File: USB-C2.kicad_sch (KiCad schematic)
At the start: 85 parts, among them J4 USB_C_Receptacle, J5 I2C2_TPS, J6 I2C, SW2 FW_Upgrade, U10 M24256-BWMN6P, U11 TPD4E02B04DQA, U12 TPD4E02B04DQA, U13 TPD4E02B04DQA, U14 TUSB1142IRNQR_C5216209, U8 TVS2200DRV, U9 TPS25762CQRQLRQ1

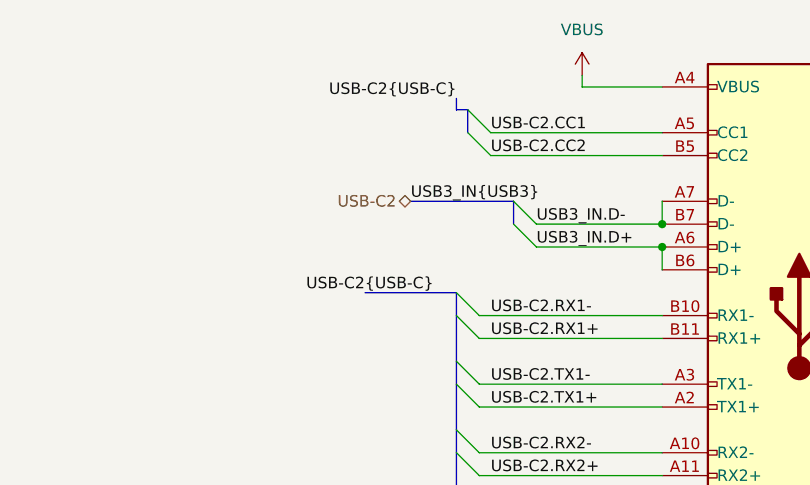
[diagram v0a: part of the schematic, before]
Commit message: labels naming fixes, USB Type E connector added
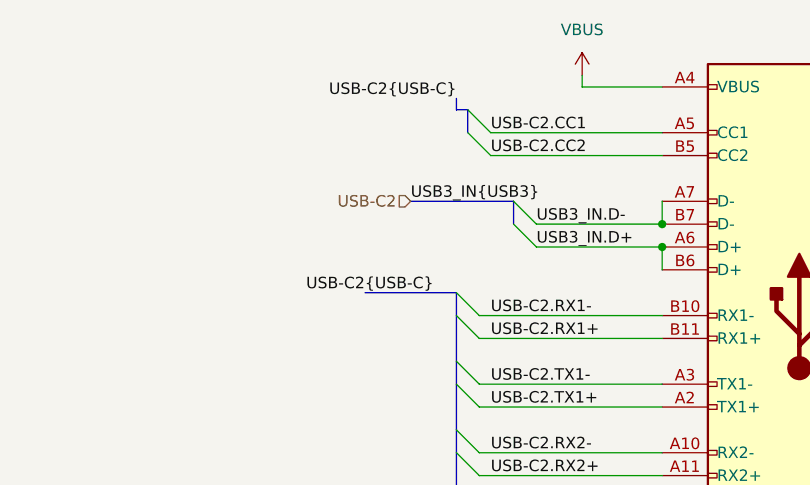
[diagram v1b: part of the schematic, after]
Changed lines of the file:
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@@
 	)
 	(hierarchical_label "USB-C2"
-		(shape bidirectional)
+		(shape input)
 		(at 334.01 34.29 180)
 		(effects

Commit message: TPS25762 EEPROM connector added
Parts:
- added J7: I2C_EEPROM, symbol Connector:Conn_01x02_Pin
- added R26: 1k DNP, symbol Device:R
- J5: value I2C2_TPS -> I2C2_PD_Controller
- J6: value I2C -> I2C_Mux
- renumbered C46 to C45, C45 to C46, C54 to C53, C55 to C54, C53 to C55, R13 to R12, R14 to R13, R15 to R14, R16 to R15, R17 to R16, R18 to R17, R21 to R18, R22 to R21, R23 to R22, R24 to R23, R25 to R24, R26 to R25, R35 to R27, R27 to R28, R28 to R29, R29 to R30, R36 to R31, R37 to R32, R30 to R33, R31 to R34, R32 to R35, R38 to R36, R39 to R37, R33 to R38, R34 to R39
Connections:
- net +3V3: now also R26.2
- net AEQCFG: now also R31.2, R36.2
- net AEQENZ: no longer R31.2, R36.2
- net EEPROM_TPS.SCL: now also J7.2 (Pin_2)
- net EEPROM_TPS.SDA: now also J7.1 (Pin_1)
- net MODE: now also R26.1
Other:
- note added: "Configuration Pins"
- note added: "Decoupling capacitors"
- note added: "EEPROM for PD Controller"
- note added: "ESD Protection"
- note added: "I2C EEPROM"
- note added: "I2C Mux"
- note added: "I2C PD Controller"
- note added: "I2C mode"
- note added: "PD Controller"
- note added: "Pin-stap mode"
- note added: "Port USB"
- note added: "USB Mux"
- title: (none) -> USB Hub
- moved on the sheet: C33, C34, C35, C36, C37, C38, C39, C40, C41, C42, C43, C45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

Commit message: deleted duplicated capacitor
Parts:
- C31, C33, C35, C39, C40, C41, C42, C43, C44, C45, C46, C47, C48, C51, C52, C53, C54, C56, C57, C58, C59, C60, C61, C62, C63, C65, C66, C67, C68: footprint (none) -> Capacitor_SMD:C_0402_1005Metric
- C32, C34, C36, C38, C55: footprint 22uF -> Capacitor_SMD:C_0402_1005Metric
- C37, C49, C50, C64: footprint (none) -> Capacitor_THT:C_Radial_D10.0mm_H16.0mm_P5.00mm
- J4: footprint (none) -> Connector_USB:USB_C_Receptacle_Amphenol_12401610E4-2A
- J5, J6, J7, TH1: footprint (none) -> Connector_PinHeader_1.27mm:PinHeader_1x02_P1.27mm_Vertical
- L1: footprint (none) -> Inductor_SMD:L_6.3x6.3_H3
- NT1, R12, R13, R14, R15, R16, R17, R18, R19, R20, R21, R22, R23, R24, R25, R27, R28, R29, R30, R31, R32, R33, R34, R35, R36, R37, R38, R39, R40, R41, R42, R43: footprint (none) -> Resistor_SMD:R_0603_1608Metric
- R26: footprint (none) -> Resistor_SMD:R_0603_1608Metric; now not fitted
- SW2: footprint (none) -> Button_Switch_SMD:SW_Push_1P1T_XKB_TS-1187A
- TP3, TP4: footprint (none) -> TestPoint:TestPoint_THTPad_1.5x1.5mm_Drill0.7mm

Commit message: Minor fixes
Fixed unclear labelling of buses
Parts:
- R12, R13, R14, R15, R16, R17, R18, R19, R20, R21, R22, R24, R25, R26, R27, R28, R29, R30, R31, R32, R33, R34, R35, R36, R37, R38, R39, R40, R41, R42, R43: footprint Resistor_SMD:R_0603_1608Metric -> Resistor_SMD:R_0402_1005Metric
- R23: footprint Resistor_SMD:R_0603_1608Metric -> Resistor_SMD:R_1206_3216Metric
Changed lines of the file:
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@@
 			)
 		)
-		(property "Footprint" "Resistor_SMD:R_0603_1608Metric"
+		(property "Footprint" "Resistor_SMD:R_0402_1005Metric"
 			(at 214.63 66.802 90)
 			(effects
@@
 			)
 		)
-		(property "Footprint" "Resistor_SMD:R_0603_1608Metric"
+		(property "Footprint" "Resistor_SMD:R_0402_1005Metric"
 			(at 201.422 29.21 90)
 			(effects
@@
 			)
 		)
-		(property "Footprint" "Resistor_SMD:R_0603_1608Metric"
+		(property "Footprint" "Resistor_SMD:R_0402_1005Metric"
 			(at 151.13 214.63 0)
 			(effects
@@
 			)
 		)
-		(property "Footprint" "Resistor_SMD:R_0603_1608Metric"
+		(property "Footprint" "Resistor_SMD:R_0402_1005Metric"
 			(at 154.94 217.17 0)
 			(effects
@@
 			)
 		)
-		(property "Footprint" "Resistor_SMD:R_0603_1608Metric"
+		(property "Footprint" "Resistor_SMD:R_0402_1005Metric"
 			(at 151.13 199.39 0)
 			(effects
@@
 			)
 		)
-		(property "Footprint" "Resistor_SMD:R_0603_1608Metric"
+		(property "Footprint" "Resistor_SMD:R_0402_1005Metric"
 			(at 150.622 29.21 90)
 			(effects
@@
 			)
 		)
-		(property "Footprint" "Resistor_SMD:R_0603_1608Metric"
+		(property "Footprint" "Resistor_SMD:R_0402_1005Metric"
 			(at 210.82 173.228 90)
 			(effects
@@
 			)
 		)
-		(property "Footprint" "Resistor_SMD:R_0603_1608Metric"
+		(property "Footprint" "Resistor_SMD:R_0402_1005Metric"
 			(at 122.682 73.66 90)
 			(effects
@@
 			)
 		)
-		(property "Footprint" "Resistor_SMD:R_0603_1608Metric"
+		(property "Footprint" "Resistor_SMD:R_0402_1005Metric"
 			(at 154.94 209.55 0)
 			(effects
@@
 			)
 		)
-		(property "Footprint" "Resistor_SMD:R_0603_1608Metric"
+		(property "Footprint" "Resistor_SMD:R_0402_1005Metric"
 			(at 244.348 257.81 90)
 			(effects
@@
 			)
 		)
-		(property "Footprint" "Resistor_SMD:R_0603_1608Metric"
+		(property "Footprint" "Resistor_SMD:R_0402_1005Metric"
 			(at 211.582 207.01 90)
 			(effects
@@
 			)
 		)
-		(property "Footprint" "Resistor_SMD:R_0603_1608Metric"
+		(property "Footprint" "Resistor_SMD:R_0402_1005Metric"
 			(at 122.682 64.77 90)
 			(effects
@@
 			)
 		)
-		(property "Footprint" "Resistor_SMD:R_0603_1608Metric"
+		(property "Footprint" "Resistor_SMD:R_0402_1005Metric"
 			(at 215.138 217.17 90)
 			(effects
@@
 			)
 		)
-		(property "Footprint" "Resistor_SMD:R_0603_1608Metric"
+		(property "Footprint" "Resistor_SMD:R_0402_1005Metric"
 			(at 19.812 62.23 90)
 			(effects
@@
 			)
 		)
-		(property "Footprint" "Resistor_SMD:R_0603_1608Metric"
+		(property "Footprint" "Resistor_SMD:R_0402_1005Metric"
 			(at 240.792 247.65 90)
 			(effects
@@
 			)
 		)
-		(property "Footprint" "Resistor_SMD:R_0603_1608Metric"
+		(property "Footprint" "Resistor_SMD:R_0402_1005Metric"
 			(at 108.712 29.21 90)
 			(effects
@@
 			)
 		)
-		(property "Footprint" "Resistor_SMD:R_0603_1608Metric"
+		(property "Footprint" "Resistor_SMD:R_0402_1005Metric"
 			(at 151.13 222.25 0)
 			(effects
@@
 			)
 		)
-		(property "Footprint" "Resistor_SMD:R_0603_1608Metric"
+		(property "Footprint" "Resistor_SMD:R_0402_1005Metric"
 			(at 213.36 56.642 90)
 			(effects
@@
 			)
 		)
-		(property "Footprint" "Resistor_SMD:R_0603_1608Metric"
+		(property "Footprint" "Resistor_SMD:R_0402_1005Metric"
 			(at 210.82 178.308 90)
 			(effects
@@
 			)
 		)
-		(property "Footprint" "Resistor_SMD:R_0603_1608Metric"
+		(property "Footprint" "Resistor_SMD:R_0402_1005Metric"
 			(at 127.762 29.21 90)
 			(effects
@@
 			)
 		)
-		(property "Footprint" "Resistor_SMD:R_0603_1608Metric"
+		(property "Footprint" "Resistor_SMD:R_0402_1005Metric"
 			(at 216.662 247.65 90)
 			(effects
@@
 			)
 		)
-		(property "Footprint" "Resistor_SMD:R_0603_1608Metric"
+		(property "Footprint" "Resistor_SMD:R_0402_1005Metric"
 			(at 242.062 207.01 90)
 			(effects
@@
 			)
 		)
-		(property "Footprint" "Resistor_SMD:R_0603_1608Metric"
+		(property "Footprint" "Resistor_SMD:R_0402_1005Metric"
 			(at 151.13 207.01 0)
 			(effects
@@
 			)
 		)
-		(property "Footprint" "Resistor_SMD:R_0603_1608Metric"
+		(property "Footprint" "Resistor_SMD:R_0402_1005Metric"
 			(at 154.94 201.93 0)
 			(effects
@@
 			)
 		)
-		(property "Footprint" "Resistor_SMD:R_0603_1608Metric"
+		(property "Footprint" "Resistor_SMD:R_0402_1005Metric"
 			(at 108.712 92.71 90)
 			(effects
@@
 			)
 		)
-		(property "Footprint" "Resistor_SMD:R_0603_1608Metric"
+		(property "Footprint" "Resistor_SMD:R_0402_1005Metric"
 			(at 186.182 29.21 90)
 			(effects
@@
 			)
 		)
-		(property "Footprint" "Resistor_SMD:R_0603_1608Metric"
+		(property "Footprint" "Resistor_SMD:R_1206_3216Metric"
 			(at 236.22 74.168 90)
 			(effects
@@
 			)
 		)
-		(property "Footprint" "Resistor_SMD:R_0603_1608Metric"
+		(property "Footprint" "Resistor_SMD:R_0402_1005Metric"
 			(at 154.94 224.79 0)
 			(effects
@@
 			)
 		)
-		(property "Footprint" "Resistor_SMD:R_0603_1608Metric"
+		(property "Footprint" "Resistor_SMD:R_0402_1005Metric"
 			(at 220.218 257.81 90)
 			(effects
@@
 			)
 		)
-		(property "Footprint" "Resistor_SMD:R_0603_1608Metric"
+		(property "Footprint" "Resistor_SMD:R_0402_1005Metric"
 			(at 245.618 217.17 90)
 			(effects
@@
 			)
 		)
-		(property "Footprint" "Resistor_SMD:R_0603_1608Metric"
+		(property "Footprint" "Resistor_SMD:R_0402_1005Metric"
 			(at 220.472 29.21 90)
 			(effects
@@
 			)
 		)
-		(property "Footprint" "Resistor_SMD:R_0603_1608Metric"
+		(property "Footprint" "Resistor_SMD:R_0402_1005Metric"
 			(at 37.592 62.23 90)
 			(effects

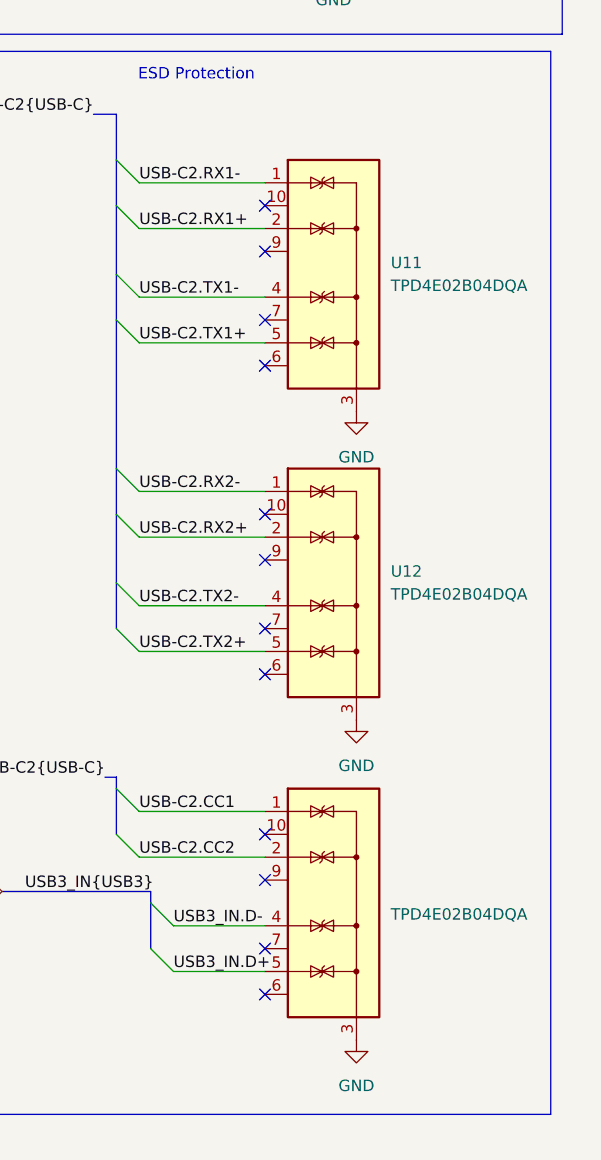
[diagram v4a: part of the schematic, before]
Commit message: Scheme fixes
Fixed wrong connection of SNS pin of U21
USB7206c symbol improved
R7's value fixed
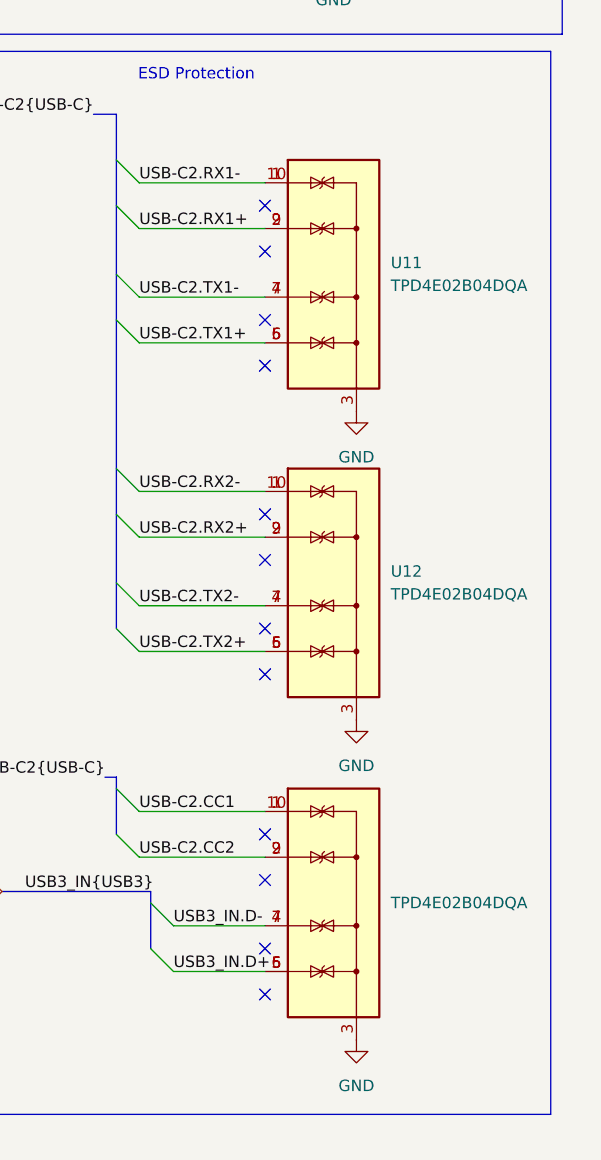
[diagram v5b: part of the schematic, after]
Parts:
- U11, U12, U13: symbol Power_Protection:TPD4E02B04DQA -> Snapeda:TPD4E02B04DQA
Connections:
- net USB-C2.CC1: now also U13.10 (NC)
- net USB-C2.CC2: now also U13.9 (NC)
- net USB-C2.RX1+: now also U11.9 (NC)
- net USB-C2.RX1-: now also U11.10 (NC)
- net USB-C2.RX2+: now also U12.9 (NC)
- net USB-C2.RX2-: now also U12.10 (NC)
- net USB-C2.TX1+: now also U11.6 (NC)
- net USB-C2.TX1-: now also U11.7 (NC)
- net USB-C2.TX2+: now also U12.6 (NC)
- net USB-C2.TX2-: now also U12.7 (NC)
- net USB3_IN.D+: now also U13.6 (NC)
- net USB3_IN.D-: now also U13.7 (NC)
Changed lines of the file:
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@@
 	)
 	(symbol
-		(lib_id "Power_Protection:TPD4E02B04DQA")
+		(lib_id "Snapeda:TPD4E02B04DQA")
 		(at 382.27 160.02 0)
 		(unit 1)
@@
 	)
 	(symbol
-		(lib_id "Power_Protection:TPD4E02B04DQA")
+		(lib_id "Snapeda:TPD4E02B04DQA")
 		(at 382.27 195.58 0)
 		(unit 1)
@@
 		)
 		(property "Value" "TPD4E02B04DQA"
-			(at 388.62 196.8499 0)
+			(at 388.62 195.5799 0)
 			(effects
 				(font
@@
 	)
 	(symbol
-		(lib_id "Power_Protection:TPD4E02B04DQA")
+		(lib_id "Snapeda:TPD4E02B04DQA")
 		(at 382.27 125.73 0)
 		(unit 1)

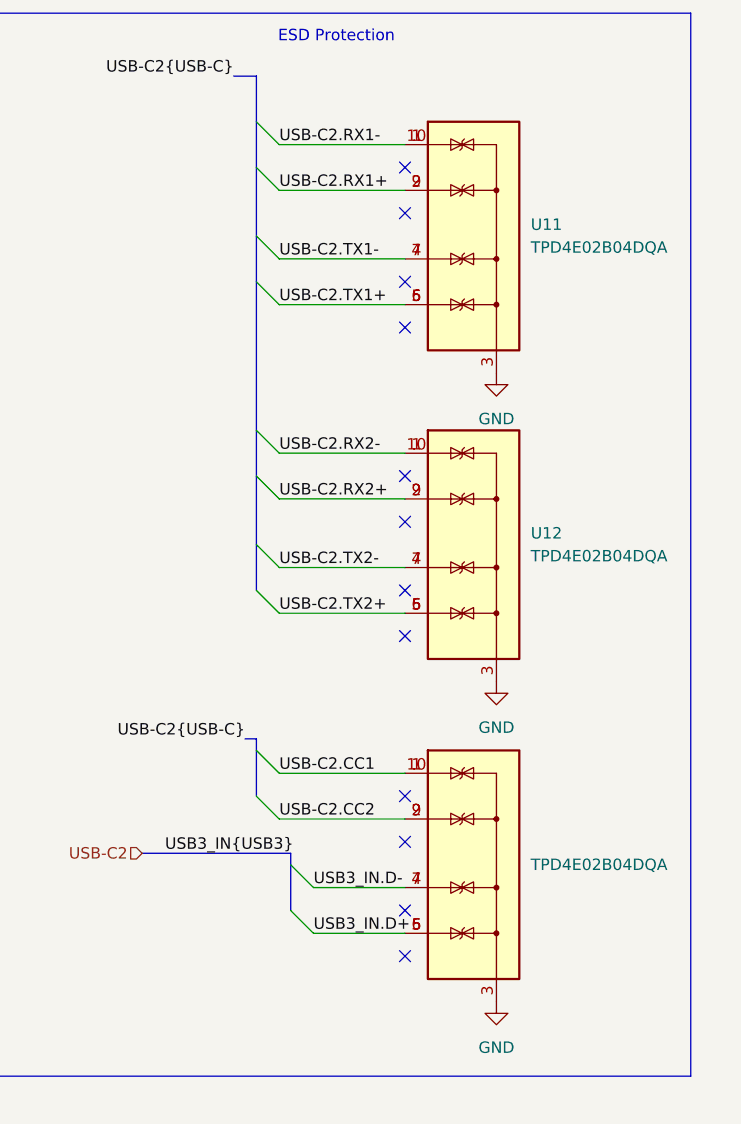
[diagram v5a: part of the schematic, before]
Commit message: MCP19035 changed to MP8795
TPS7A4701xRGW to AP7361C-33E
Led Indicator added
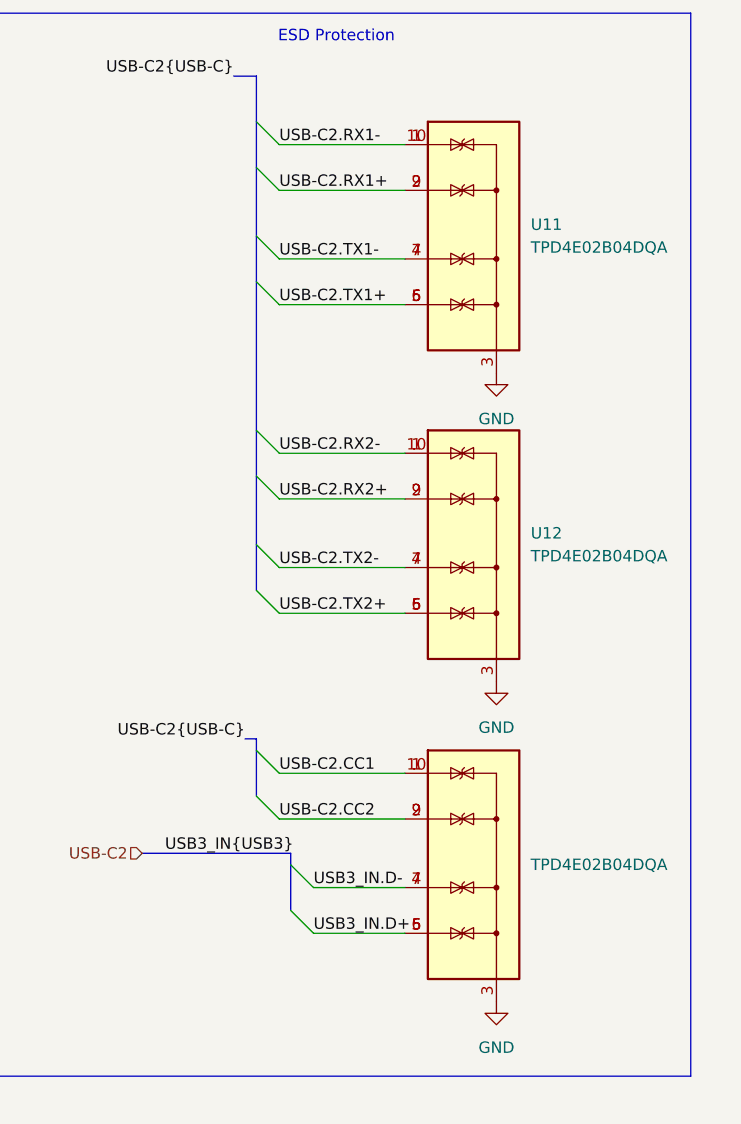
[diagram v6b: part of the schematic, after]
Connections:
- no-connect marks 26 -> 14
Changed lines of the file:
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@@
-	)
-	(no_connect
-		(at 374.65 193.04)
-	)
-	(no_connect
-		(at 374.65 170.18)
-	)
-	(no_connect
-		(at 374.65 130.81)
-	)
-	(no_connect
-		(at 374.65 205.74)
 	)
 	(no_connect
@@
 	)
 	(no_connect
-		(at 374.65 165.1)
-	)
-	(no_connect
 		(at 363.22 81.28)
-	)
-	(no_connect
-		(at 374.65 187.96)
-	)
-	(no_connect
-		(at 374.65 135.89)
 	)
 	(no_connect
@@
 	)
 	(no_connect
-		(at 374.65 200.66)
-	)
-	(no_connect
 		(at 82.55 227.33)
 	)
@@
 	)
 	(no_connect
-		(at 374.65 152.4)
-	)
-	(no_connect
-		(at 374.65 157.48)
-	)
-	(no_connect
-		(at 374.65 123.19)
-	)
-	(no_connect
 		(at 123.19 240.03)
 	)
 	(no_connect
-		(at 374.65 118.11)
-	)
-	(no_connect

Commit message: I2C Addresses added to scheme
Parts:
- added R47, R50, R51, R52: 4.7k, Resistor_SMD:R_0402_1005Metric, symbol Device:R
- C41, C43: value 0.1uF (10V) -> 0.1uF (50V)
- R25: value R -> 1k
- U10: value M24256-BWMN6P -> 24LC256
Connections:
- net +3V3: now also R51.1, R52.1
- net +3V3_LDO: now also R47.1, R50.1
- net EEPROM_TPS.SCL: now also R51.2
- net EEPROM_TPS.SDA: now also R52.2
- net I2C2_TPS.SCL: now also R47.2
- net I2C2_TPS.SDA: now also R50.2
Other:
- note added: "Address can be choosen during configuration"
- note added: "Address will be known after routing"
- note added: "I2C2 (target) PD Controller"
- note added: "Need to be flashed before use"
- note removed: "I2C PD Controller"
- note removed: "Target adress: 0x50"
- moved on the sheet: C55, R25, TH1
